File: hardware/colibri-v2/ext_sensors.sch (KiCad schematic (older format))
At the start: 20 parts

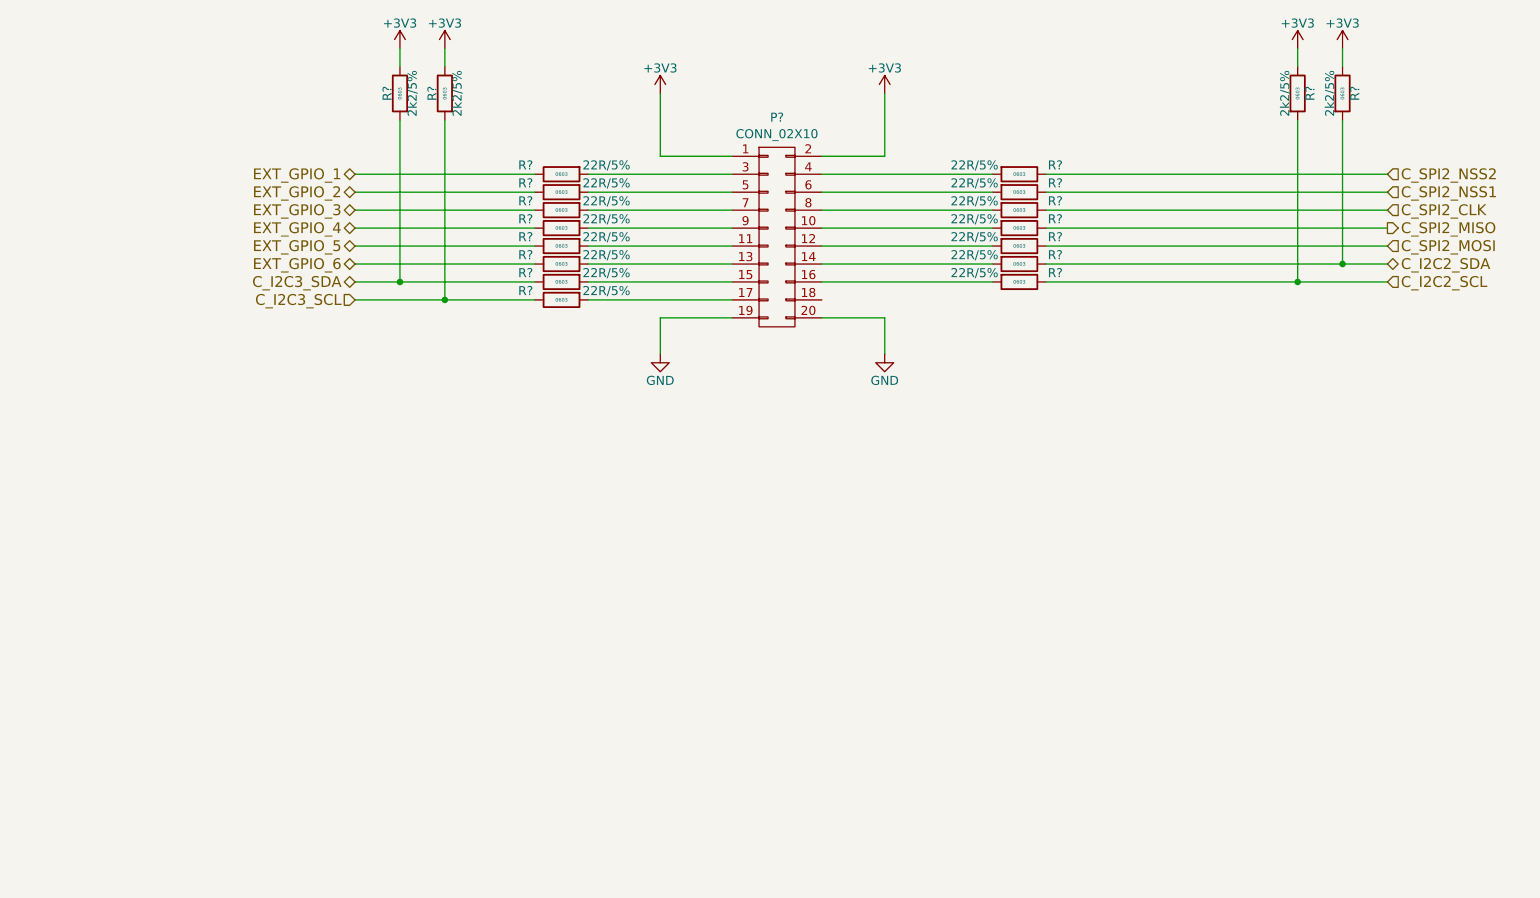
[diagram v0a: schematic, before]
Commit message: Added wurth connector to the expansion sheet.
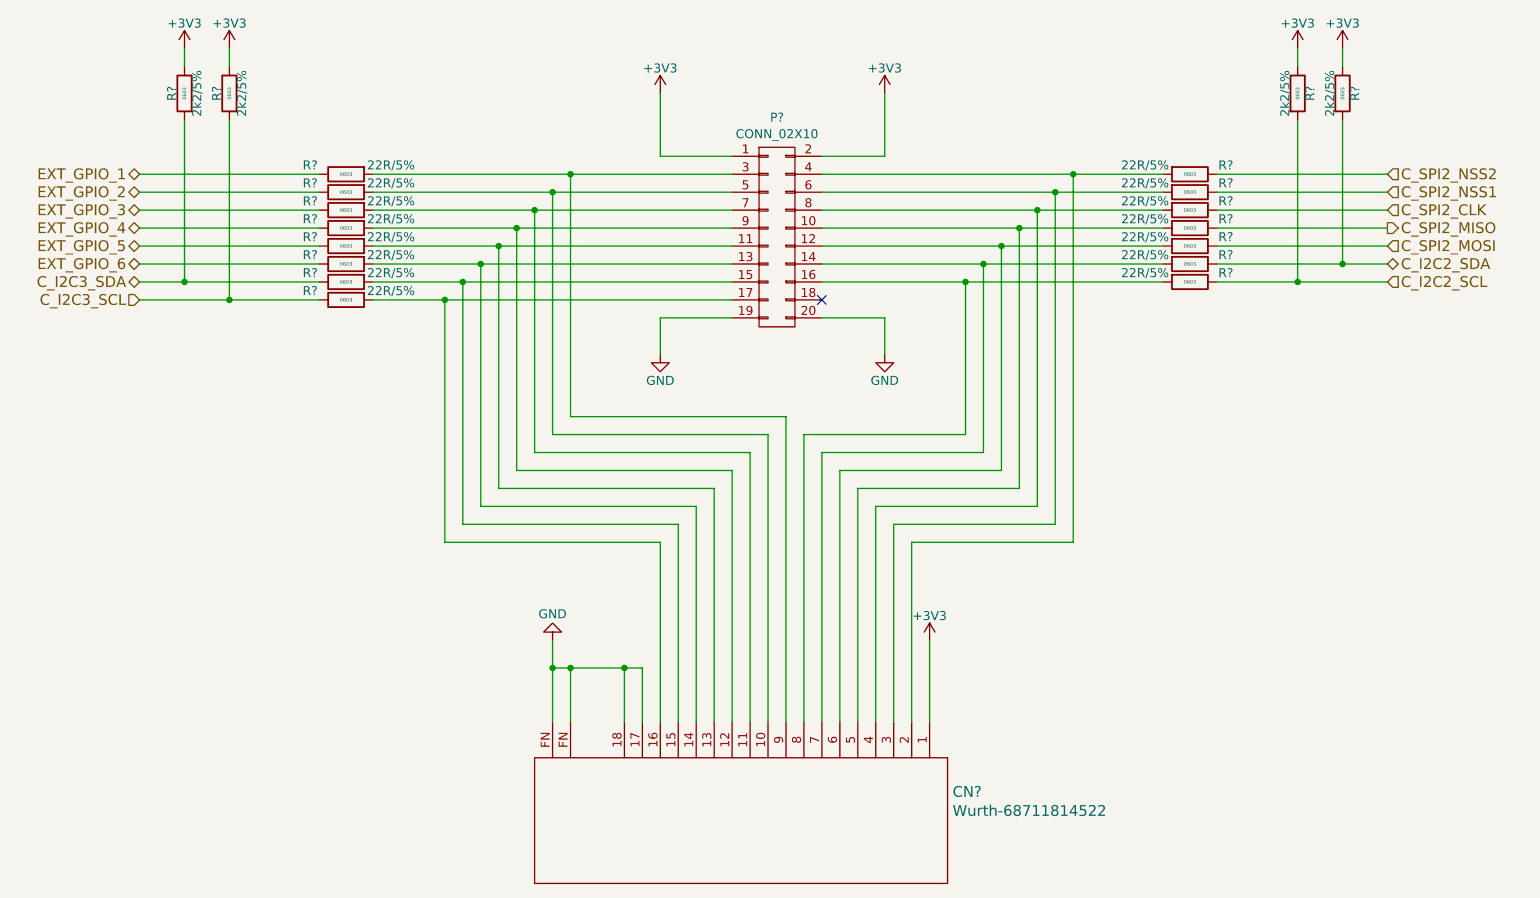
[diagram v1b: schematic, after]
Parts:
- added CN?: Wurth-68711814522, symbol Wurth-68711814522
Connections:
- net +3V3: now also CN?.1
- net GND: now also CN?.17, CN?.18, CN?.FN
- net at P?.4 (P4), R?.2: now also CN?.2
- net at P?.6 (P6), R?.2: now also CN?.3
- net at P?.8 (P8), R?.2: now also CN?.4
- net at P?.10 (P10), R?.2: now also CN?.5
- net at P?.12 (P12), R?.2: now also CN?.6
- net at P?.14 (P14), R?.2: now also CN?.7
- net at P?.16 (P16), R?.2: now also CN?.8
- net at P?.15 (P15), R?.2: now also CN?.15
- net at P?.17 (P17), R?.2: now also CN?.16
- net at P?.11 (P11), R?.2: now also CN?.13
- net at P?.13 (P13), R?.2: now also CN?.14
- net at P?.3 (P3), R?.2: now also CN?.9
- net at P?.5 (P5), R?.2: now also CN?.10
- net at P?.7 (P7), R?.2: now also CN?.11
- net at P?.9 (P9), R?.2: now also CN?.12
- no-connect marks 0 -> 1
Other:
- moved on the sheet: R?

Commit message: Resolving ERC problems
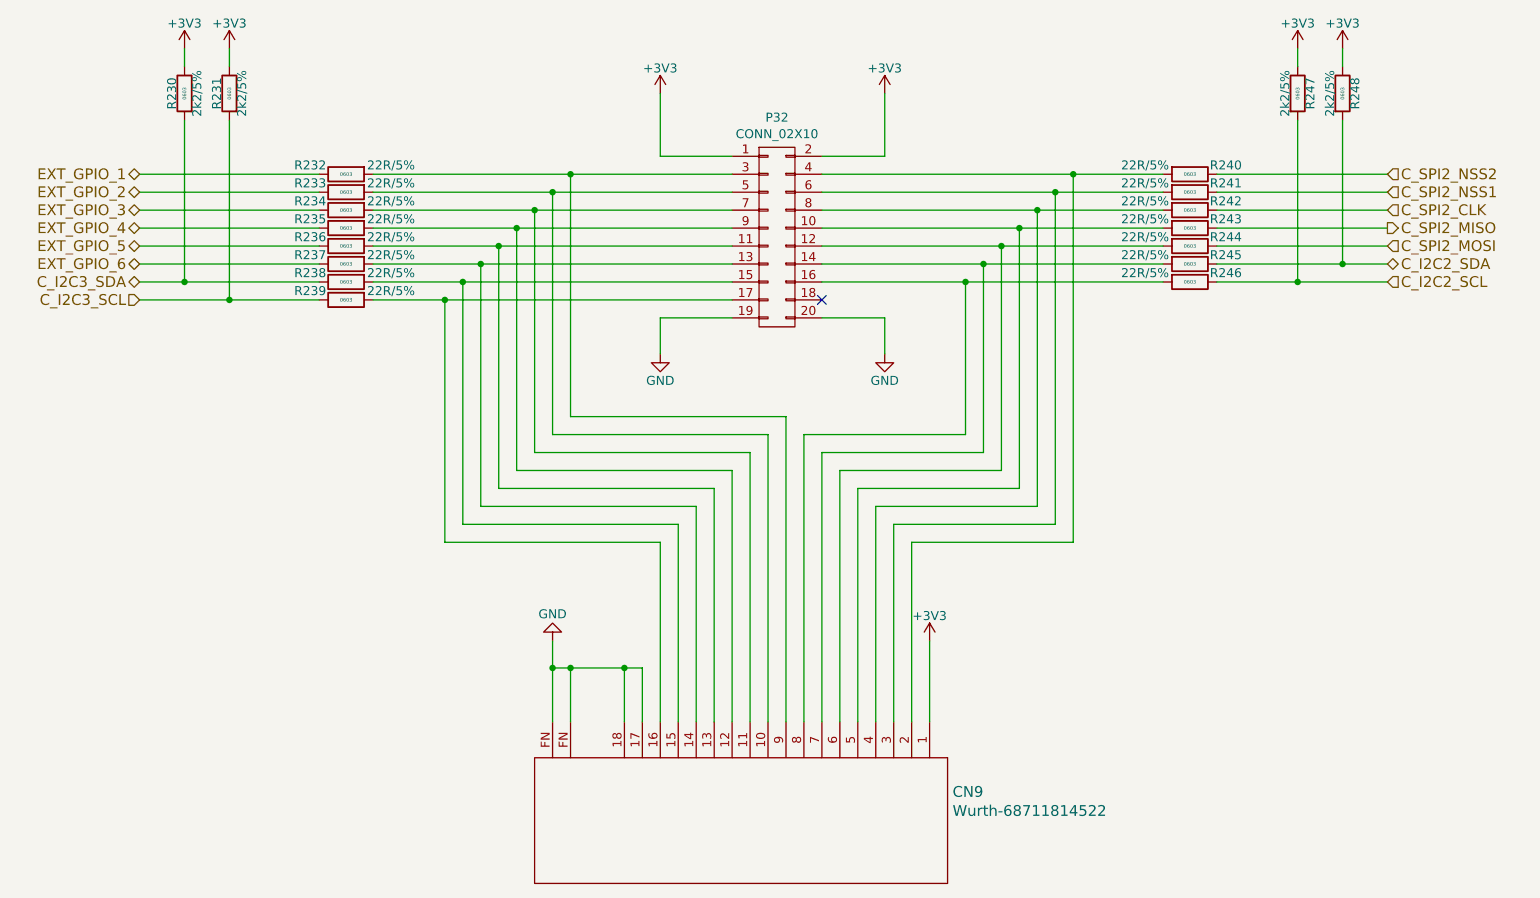
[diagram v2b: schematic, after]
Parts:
- gave numbers to parts that had none: 21
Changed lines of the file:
@@
 EESchema Schematic File Version 2
+LIBS:colibri-wnd-rescue
 LIBS:power
 LIBS:device
@@
 $EndDescr
 $Comp
-L GND #PWR?
+L GND #PWR0329
 U 1 1 56D0AF0F
 P 6050 3550
-F 0 "#PWR?" H 6050 3300 50  0001 C CNN
+F 0 "#PWR0329" H 6050 3300 50  0001 C CNN
 F 1 "GND" H 6050 3400 50  0000 C CNN
 F 2 "" H 6050 3550 60  0000 C CNN
@@
 $EndComp
 $Comp
-L +3V3 #PWR?
+L +3V3 #PWR0330
 U 1 1 56D0AF21
 P 6050 2100
-F 0 "#PWR?" H 6050 1950 50  0001 C CNN
+F 0 "#PWR0330" H 6050 1950 50  0001 C CNN
 F 1 "+3V3" H 6050 2240 50  0000 C CNN
 F 2 "" H 6050 2100 60  0000 C CNN
@@
 $EndComp
 $Comp
-L R_SMT R?
+L R_SMT R240
 U 1 1 56D0AF46
 P 7750 2550
-F 0 "R?" V 7700 2750 50  0000 C CNN
+F 0 "R240" V 7700 2750 50  0000 C CNN
 F 1 "22R/5%" V 7700 2300 50  0000 C CNN
 F 2 "Resistors_SMD:R_0603" V 7900 2550 30  0001 C CNN
@@
 $EndComp
 $Comp
-L R_SMT R?
+L R_SMT R241
 U 1 1 56D0AF50
 P 7750 2650
-F 0 "R?" V 7700 2850 50  0000 C CNN
+F 0 "R241" V 7700 2850 50  0000 C CNN
 F 1 "22R/5%" V 7700 2400 50  0000 C CNN
 F 2 "Resistors_SMD:R_0603" V 7900 2650 30  0001 C CNN
@@
 $EndComp
 $Comp
-L R_SMT R?
+L R_SMT R242
 U 1 1 56D0AF5A
 P 7750 2750
-F 0 "R?" V 7700 2950 50  0000 C CNN
+F 0 "R242" V 7700 2950 50  0000 C CNN
 F 1 "22R/5%" V 7700 2500 50  0000 C CNN
 F 2 "Resistors_SMD:R_0603" V 7900 2750 30  0001 C CNN
@@
 $EndComp
 $Comp
-L R_SMT R?
+L R_SMT R243
 U 1 1 56D0AF64
 P 7750 2850
-F 0 "R?" V 7700 3050 50  0000 C CNN
+F 0 "R243" V 7700 3050 50  0000 C CNN
 F 1 "22R/5%" V 7700 2600 50  0000 C CNN
 F 2 "Resistors_SMD:R_0603" V 7900 2850 30  0001 C CNN
@@
 $EndComp
 $Comp
-L R_SMT R?
+L R_SMT R244
 U 1 1 56D0AF6E
 P 7750 2950
-F 0 "R?" V 7700 3150 50  0000 C CNN
+F 0 "R244" V 7700 3150 50  0000 C CNN
 F 1 "22R/5%" V 7700 2700 50  0000 C CNN
 F 2 "Resistors_SMD:R_0603" V 7900 2950 30  0001 C CNN
@@
 $EndComp
 $Comp
-L R_SMT R?
+L R_SMT R245
 U 1 1 56D0AF8C
 P 7750 3050
-F 0 "R?" V 7700 3250 50  0000 C CNN
+F 0 "R245" V 7700 3250 50  0000 C CNN
 F 1 "22R/5%" V 7700 2800 50  0000 C CNN
 F 2 "Resistors_SMD:R_0603" V 7900 3050 30  0001 C CNN
@@
 $EndComp
 $Comp
-L R_SMT R?
+L R_SMT R246
 U 1 1 56D0AF96
 P 7750 3150
-F 0 "R?" V 7700 3350 50  0000 C CNN
+F 0 "R246" V 7700 3350 50  0000 C CNN
 F 1 "22R/5%" V 7700 2900 50  0000 C CNN
 F 2 "Resistors_SMD:R_0603" V 7900 3150 30  0001 C CNN
@@
 C_I2C2_SCL
 $Comp
-L +3V3 #PWR?
+L +3V3 #PWR0331
 U 1 1 56D120DB
 P 8350 1850
-F 0 "#PWR?" H 8350 1700 50  0001 C CNN
+F 0 "#PWR0331" H 8350 1700 50  0001 C CNN
 F 1 "+3V3" H 8350 1990 50  0000 C CNN
 F 2 "" H 8350 1850 60  0000 C CNN
@@
 $EndComp
 $Comp
-L +3V3 #PWR?
+L +3V3 #PWR0332
 U 1 1 56D120E1
 P 8600 1850
-F 0 "#PWR?" H 8600 1700 50  0001 C CNN
+F 0 "#PWR0332" H 8600 1700 50  0001 C CNN
 F 1 "+3V3" H 8600 1990 50  0000 C CNN
 F 2 "" H 8600 1850 60  0000 C CNN
@@
 $EndComp
 $Comp
-L R_SMT R?
+L R_SMT R248
 U 1 1 56D120EE
 P 8600 2100
-F 0 "R?" V 8670 2100 50  0000 C CNN
+F 0 "R248" V 8670 2100 50  0000 C CNN
 F 1 "2k2/5%" V 8530 2100 50  0000 C CNN
 F 2 "Resistors_SMD:R_0603" V 8750 2100 30  0001 C CNN
@@
 $EndComp
 $Comp
-L R_SMT R?
+L R_SMT R247
 U 1 1 56D120F8
 P 8350 2100
-F 0 "R?" V 8420 2100 50  0000 C CNN
+F 0 "R247" V 8420 2100 50  0000 C CNN
 F 1 "2k2/5%" V 8280 2100 50  0000 C CNN
 F 2 "Resistors_SMD:R_0603" V 8500 2100 30  0001 C CNN
@@
 $EndComp
 $Comp
-L R_SMT R?
+L R_SMT R238
 U 1 1 56D12651
 P 3050 3150
-F 0 "R?" V 3000 3350 50  0000 C CNN
+F 0 "R238" V 3000 3350 50  0000 C CNN
 F 1 "22R/5%" V 3000 2900 50  0000 C CNN
 F 2 "Resistors_SMD:R_0603" V 3200 3150 30  0001 C CNN
@@
 $EndComp
 $Comp
-L R_SMT R?
+L R_SMT R239
 U 1 1 56D1265A
 P 3050 3250
-F 0 "R?" V 3000 3450 50  0000 C CNN
+F 0 "R239" V 3000 3450 50  0000 C CNN
 F 1 "22R/5%" V 3000 3000 50  0000 C CNN
 F 2 "Resistors_SMD:R_0603" V 3200 3250 30  0001 C CNN
@@
 C_I2C3_SCL
 $Comp
-L +3V3 #PWR?
+L +3V3 #PWR0333
 U 1 1 56D12668
 P 2400 1850
-F 0 "#PWR?" H 2400 1700 50  0001 C CNN
+F 0 "#PWR0333" H 2400 1700 50  0001 C CNN
 F 1 "+3V3" H 2400 1990 50  0000 C CNN
 F 2 "" H 2400 1850 60  0000 C CNN
@@
 $EndComp
 $Comp
-L +3V3 #PWR?
+L +3V3 #PWR0334
 U 1 1 56D1266E
 P 2150 1850
-F 0 "#PWR?" H 2150 1700 50  0001 C CNN
+F 0 "#PWR0334" H 2150 1700 50  0001 C CNN
 F 1 "+3V3" H 2150 1990 50  0000 C CNN
 F 2 "" H 2150 1850 60  0000 C CNN
@@
 $EndComp
 $Comp
-L R_SMT R?
+L R_SMT R230
 U 1 1 56D1267B
 P 2150 2100
-F 0 "R?" V 2220 2100 50  0000 C CNN
+F 0 "R230" V 2220 2100 50  0000 C CNN
 F 1 "2k2/5%" V 2080 2100 50  0000 C CNN
 F 2 "Resistors_SMD:R_0603" V 2300 2100 30  0001 C CNN
@@
 $EndComp
 $Comp
-L R_SMT R?
+L R_SMT R231
 U 1 1 56D12684
 P 2400 2100
-F 0 "R?" V 2470 2100 50  0000 C CNN
+F 0 "R231" V 2470 2100 50  0000 C CNN
 F 1 "2k2/5%" V 2330 2100 50  0000 C CNN
 F 2 "Resistors_SMD:R_0603" V 2550 2100 30  0001 C CNN
@@
 $EndComp
 $Comp
-L GND #PWR?
+L GND #PWR0335
 U 1 1 56D1452C
 P 4800 3550
-F 0 "#PWR?" H 4800 3300 50  0001 C CNN
+F 0 "#PWR0335" H 4800 3300 50  0001 C CNN
 F 1 "GND" H 4800 3400 50  0000 C CNN
 F 2 "" H 4800 3550 60  0000 C CNN
@@
 $EndComp
 $Comp
-L +3V3 #PWR?
+L +3V3 #PWR0336
 U 1 1 56D14567
 P 4800 2100
-F 0 "#PWR?" H 4800 1950 50  0001 C CNN
+F 0 "#PWR0336" H 4800 1950 50  0001 C CNN
 F 1 "+3V3" H 4800 2240 50  0000 C CNN
 F 2 "" H 4800 2100 60  0000 C CNN
@@
 EXT_GPIO_6
 $Comp
-L CONN_02X10 P?
+L CONN_02X10 P32
 U 1 1 56D14A48
 P 5450 2900
-F 0 "P?" H 5450 3566 50  0000 C CNN
+F 0 "P32" H 5450 3566 50  0000 C CNN
 F 1 "CONN_02X10" H 5450 3474 50  0000 C CNN
 F 2 "" H 5450 1700 50  0000 C CNN
@@
 $EndComp
 $Comp
-L R_SMT R?
+L R_SMT R236
 U 1 1 56D169EA
 P 3050 2950
-F 0 "R?" V 3000 3150 50  0000 C CNN
+F 0 "R236" V 3000 3150 50  0000 C CNN
 F 1 "22R/5%" V 3000 2700 50  0000 C CNN
 F 2 "Resistors_SMD:R_0603" V 3200 2950 30  0001 C CNN
@@
 $EndComp
 $Comp
-L R_SMT R?
+L R_SMT R237
 U 1 1 56D169F3
 P 3050 3050
-F 0 "R?" V 3000 3250 50  0000 C CNN
+F 0 "R237" V 3000 3250 50  0000 C CNN
 F 1 "22R/5%" V 3000 2800 50  0000 C CNN
 F 2 "Resistors_SMD:R_0603" V 3200 3050 30  0001 C CNN
@@
 $EndComp
 $Comp
-L R_SMT R?
+L R_SMT R234
 U 1 1 56D16ABE
 P 3050 2750
-F 0 "R?" V 3000 2950 50  0000 C CNN
+F 0 "R234" V 3000 2950 50  0000 C CNN
 F 1 "22R/5%" V 3000 2500 50  0000 C CNN
 F 2 "Resistors_SMD:R_0603" V 3200 2750 30  0001 C CNN
@@
 $EndComp
 $Comp
-L R_SMT R?
+L R_SMT R235
 U 1 1 56D16AC7
 P 3050 2850
-F 0 "R?" V 3000 3050 50  0000 C CNN
+F 0 "R235" V 3000 3050 50  0000 C CNN
 F 1 "22R/5%" V 3000 2600 50  0000 C CNN
 F 2 "Resistors_SMD:R_0603" V 3200 2850 30  0001 C CNN
@@
 $EndComp
 $Comp
-L R_SMT R?
+L R_SMT R232
 U 1 1 56D16B2A
 P 3050 2550
-F 0 "R?" V 3000 2750 50  0000 C CNN
+F 0 "R232" V 3000 2750 50  0000 C CNN
 F 1 "22R/5%" V 3000 2300 50  0000 C CNN
 F 2 "Resistors_SMD:R_0603" V 3200 2550 30  0001 C CNN
@@
 $EndComp
 $Comp
-L R_SMT R?
+L R_SMT R233
 U 1 1 56D16B33
 P 3050 2650
-F 0 "R?" V 3000 2850 50  0000 C CNN
+F 0 "R233" V 3000 2850 50  0000 C CNN
 F 1 "22R/5%" V 3000 2400 50  0000 C CNN
 F 2 "Resistors_SMD:R_0603" V 3200 2650 30  0001 C CNN
@@
 $EndComp
 $Comp
-L Wurth-68711814522 CN?
+L Wurth-68711814522 CN9
 U 1 1 56CBA246
 P 5250 6150
-F 0 "CN?" V 5090 7328 60  0000 L CNN
+F 0 "CN9" V 5090 7328 60  0000 L CNN
 F 1 "Wurth-68711814522" V 5196 7328 60  0000 L CNN
 F 2 "" H 5250 4900 60  0000 C CNN
@@
 NoConn ~ 5700 3250
 $Comp
-L +3V3 #PWR?
+L +3V3 #PWR0337
 U 1 1 56CBB9FD
 P 6300 5150
-F 0 "#PWR?" H 6300 5000 50  0001 C CNN
+F 0 "#PWR0337" H 6300 5000 50  0001 C CNN
 F 1 "+3V3" H 6300 5290 50  0000 C CNN
 F 2 "" H 6300 5150 60  0000 C CNN
@@
 $EndComp
 $Comp
-L GND #PWR?
+L GND #PWR0338
 U 1 1 56CBBB13
 P 4200 5150
-F 0 "#PWR?" H 4200 4900 50  0001 C CNN
+F 0 "#PWR0338" H 4200 4900 50  0001 C CNN
 F 1 "GND" H 4200 5000 50  0000 C CNN
 F 2 "" H 4200 5150 60  0000 C CNN
